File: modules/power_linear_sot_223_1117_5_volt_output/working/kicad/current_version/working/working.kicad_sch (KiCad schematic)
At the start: 5 parts, among them U2 pms22311171d5v

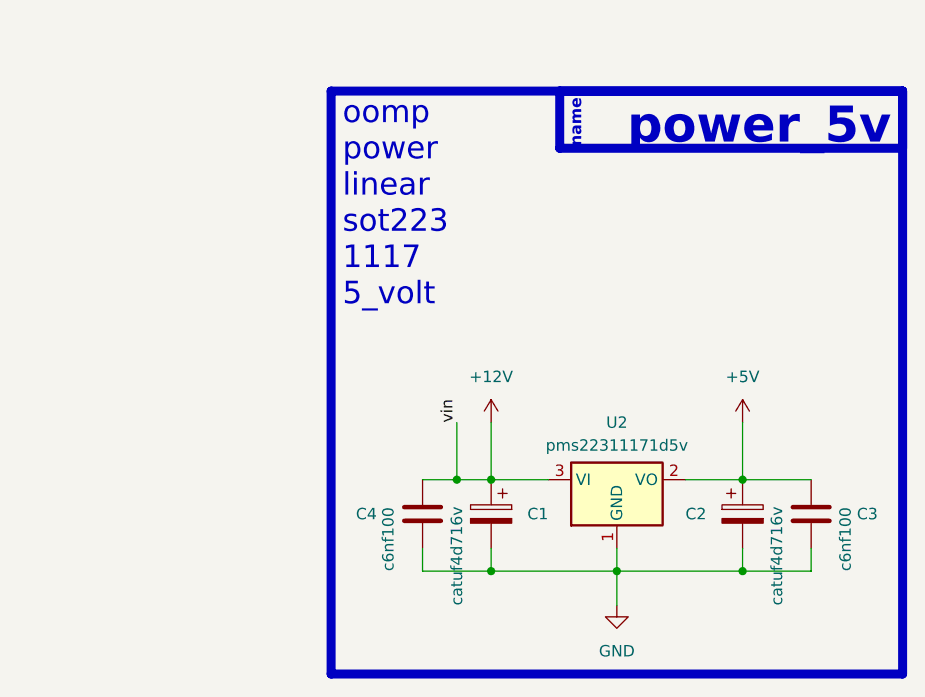
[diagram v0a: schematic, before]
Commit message: fixed formatting to be more consistent
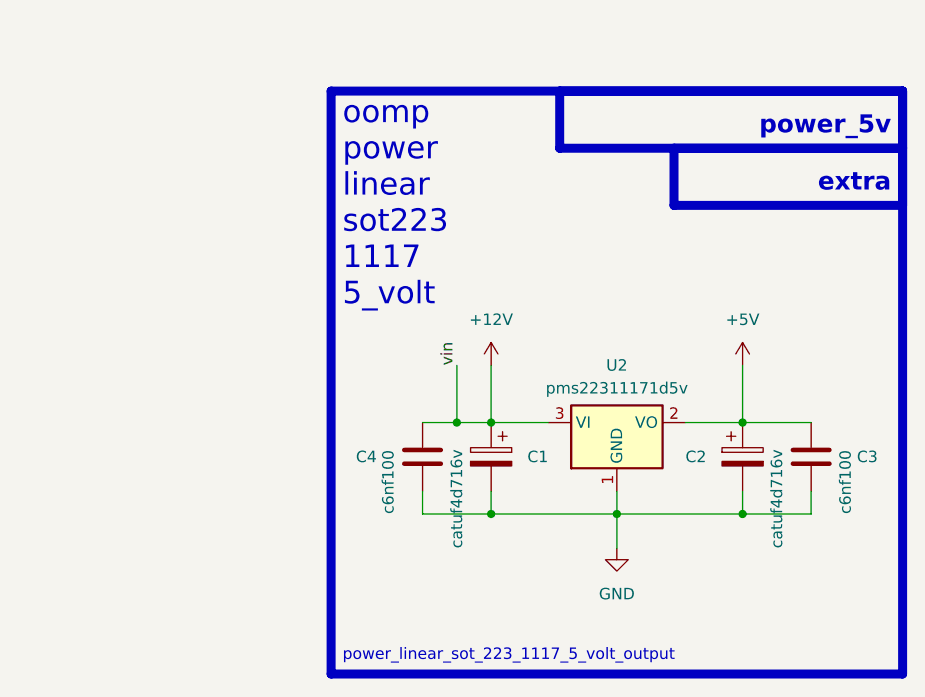
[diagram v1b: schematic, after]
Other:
- note added: "extra"
- note added: "power_linear_sot_223_1117_5_volt_output"
- note removed: "name"
- moved on the sheet: C1, C2, C3, C4, U2

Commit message: schematic formatting
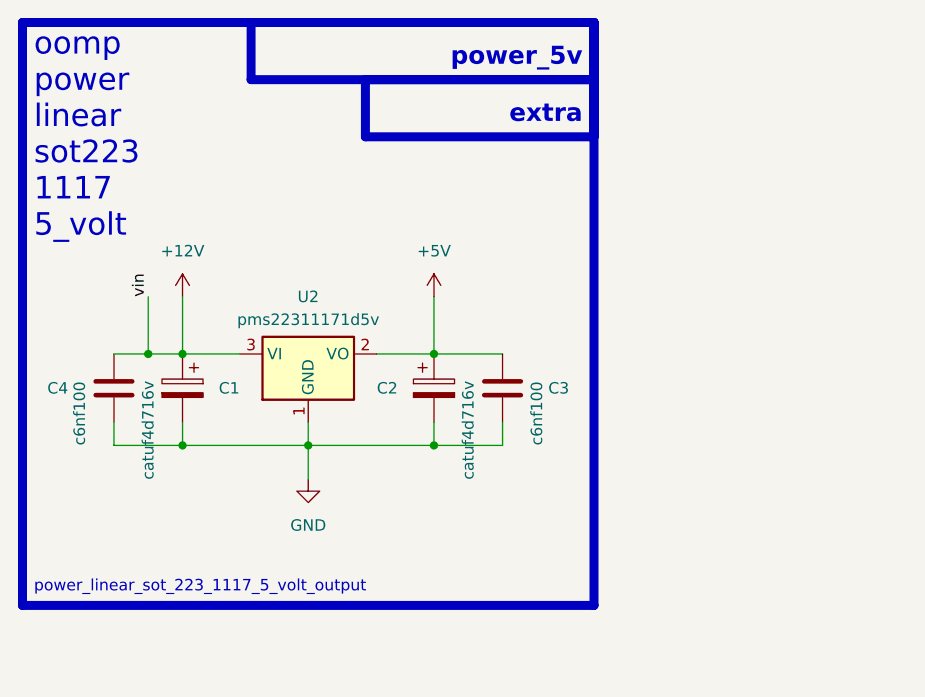
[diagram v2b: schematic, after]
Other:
- moved on the sheet: C1, C2, C3, C4, U2
